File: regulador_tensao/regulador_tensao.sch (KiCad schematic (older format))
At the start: 6 parts, among them P1 CONN_IN_5V, P2 CONN_OUT_3V3, U1 SPX3819M5-L-3-3

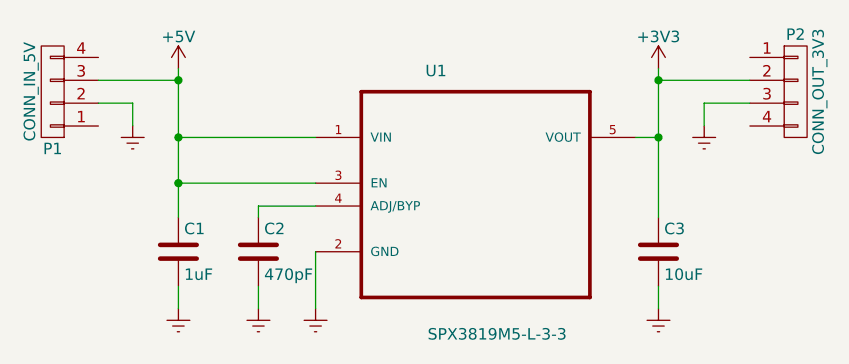
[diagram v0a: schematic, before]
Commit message: Reg. tensao finished, with renderings. Minor fixes in usb-serial
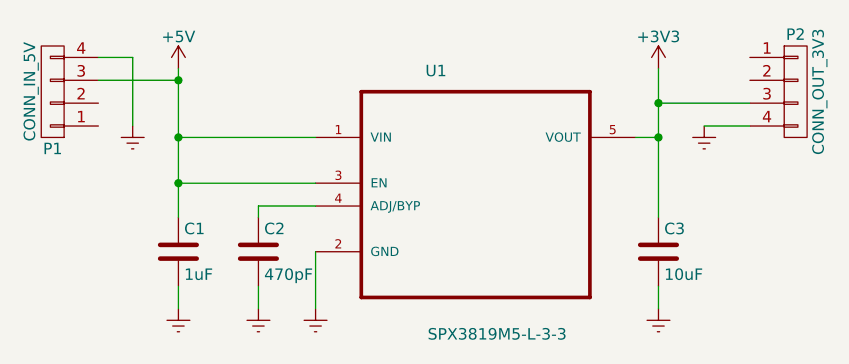
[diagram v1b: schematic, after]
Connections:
- net +3V3: now also P2.3 (P3); no longer P2.2 (P2)
- net Earth: now also P1.4 (P4), P2.4 (P4); no longer P1.2 (P2), P2.3 (P3)
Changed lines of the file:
@@
 	1    0    0    -1
 $EndComp
-Wire Wire Line
-	4400 2250 4400 2900
-Wire Wire Line
-	4400 2550 5000 2550
-Connection ~ 4400 2550
-Wire Wire Line
-	5000 2750 4400 2750
-Connection ~ 4400 2750
-Wire Wire Line
-	4750 2900 4750 2850
-Wire Wire Line
-	4750 2850 5000 2850
-Wire Wire Line
-	4400 3200 4400 3300
-Wire Wire Line
-	4750 3200 4750 3300
-Wire Wire Line
-	5000 3050 5000 3300
-Wire Wire Line
-	6500 2550 6400 2550
-Wire Wire Line
-	6500 2250 6500 2900
-Connection ~ 6500 2550
-Wire Wire Line
-	6500 3200 6500 3300
-Wire Wire Line
-	6900 2300 6500 2300
-Connection ~ 6500 2300
-Wire Wire Line
-	4050 2300 4400 2300
-Connection ~ 4400 2300
-Wire Wire Line
-	6700 2400 6900 2400
-Wire Wire Line
-	4050 2400 4200 2400
 $Comp
 L CONN_01X04 P1
@@
 $EndComp
 Wire Wire Line
-	4200 2400 4200 2500
+	4400 2250 4400 2900
 Wire Wire Line
-	6700 2500 6700 2400
+	4400 2550 5000 2550
+Connection ~ 4400 2550
+Wire Wire Line
+	5000 2750 4400 2750
+Connection ~ 4400 2750
+Wire Wire Line
+	4750 2900 4750 2850
+Wire Wire Line
+	4750 2850 5000 2850
+Wire Wire Line
+	4400 3200 4400 3300
+Wire Wire Line
+	4750 3200 4750 3300
+Wire Wire Line
+	5000 3050 5000 3300
+Wire Wire Line
+	6500 2550 6400 2550
+Wire Wire Line
+	6500 2250 6500 2900
+Connection ~ 6500 2550
+Wire Wire Line
+	6500 3200 6500 3300
+Wire Wire Line
+	4050 2300 4400 2300
+Connection ~ 4400 2300
+Wire Wire Line
+	4200 2500 4200 2200
+Wire Wire Line
+	4200 2200 4050 2200
+Wire Wire Line
+	6700 2500 6900 2500
+Wire Wire Line
+	6900 2400 6500 2400
+Connection ~ 6500 2400
 $EndSCHEMATC
